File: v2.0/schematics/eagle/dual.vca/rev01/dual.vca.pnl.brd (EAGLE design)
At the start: 100 x 80 mm, 30 parts, among them J1 CV1, J10 CV4, J11 IN4, J12 OUT4, J2 IN1, J3 OUT1, J4 CV2, J5 IN2, J6 OUT2, J7 CV3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

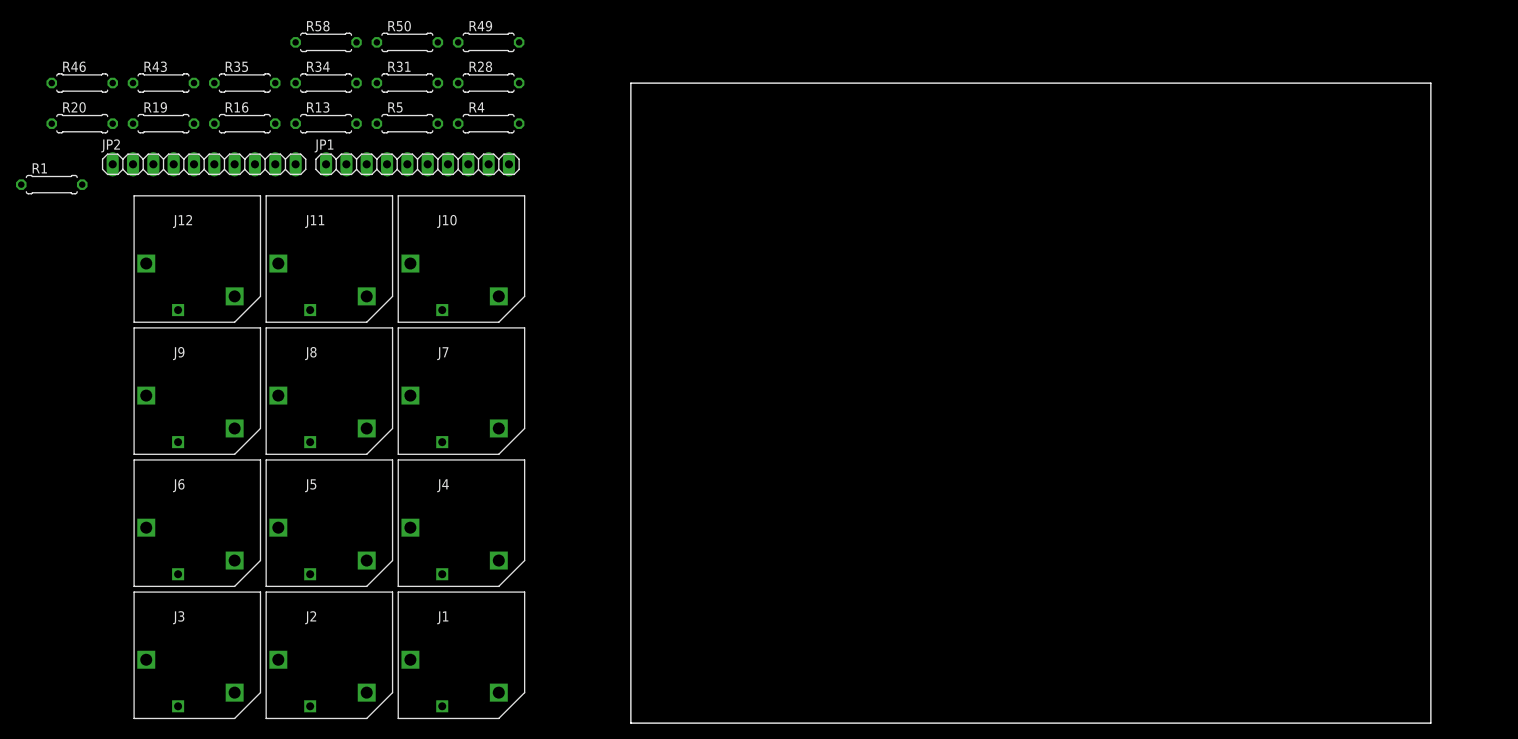
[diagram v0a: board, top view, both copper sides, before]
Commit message: Iniital board layout for main dual.vca
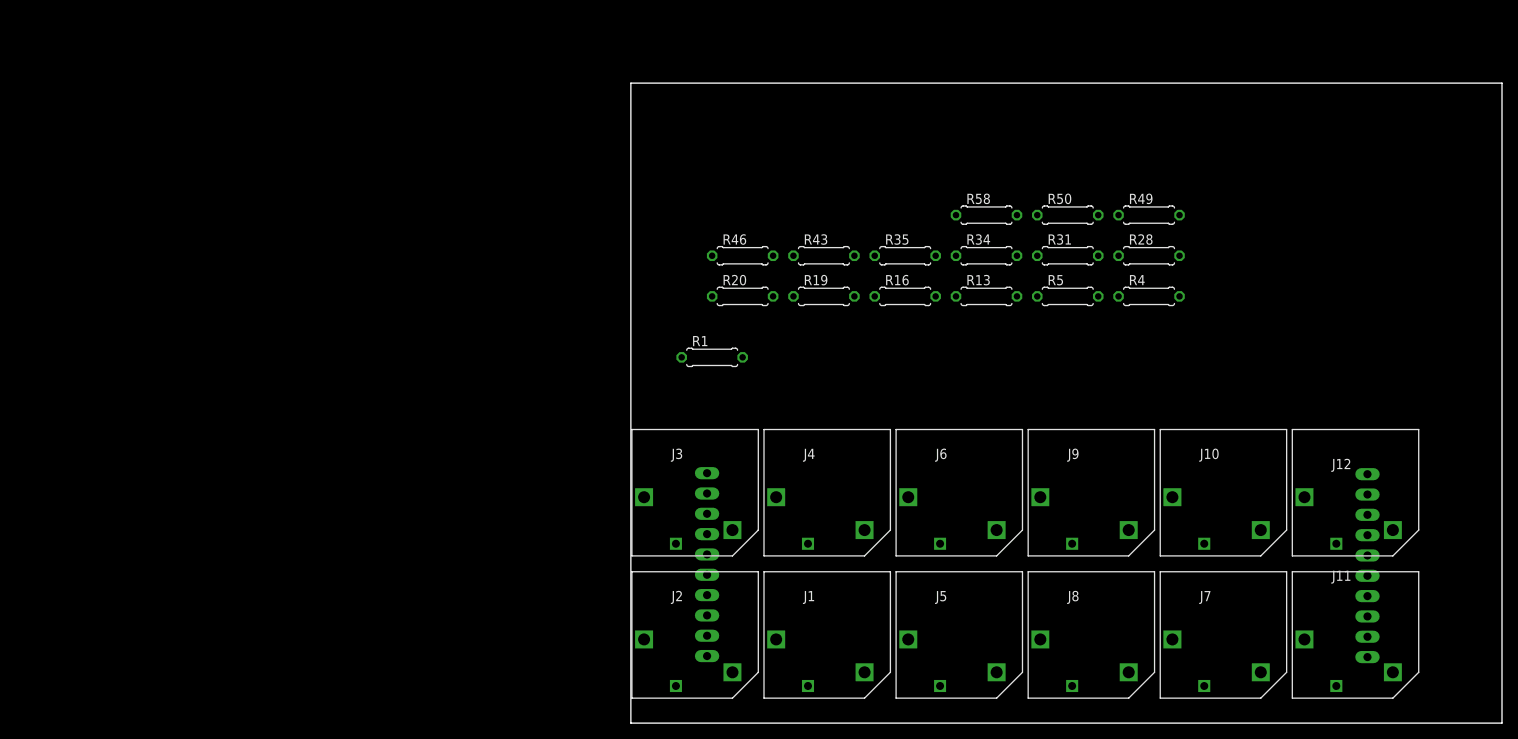
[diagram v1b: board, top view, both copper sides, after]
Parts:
- moved JP2 153.8 mm to (92.1, 19.7), flipped to the bottom, turned to 90 degrees
- moved J12 147.7 mm to (95.2, 24.1)
- moved J11 136.6 mm to (95.2, 6.35)
- moved J9 112.5 mm to (62.2, 24.1)
- moved J7 100.0 mm to (78.7, 6.35)
- moved J8 100.0 mm to (62.2, 6.35)
- moved J10 99.6 mm to (78.7, 24.1)
- moved J6 95.3 mm to (45.7, 24.1)
- moved R13 85.3 mm to (44.5, 53.3)
- moved R34 85.3 mm to (44.5, 58.4)
- moved R58 85.3 mm to (44.5, 63.5)
- moved R1 85.3 mm to (10.2, 45.7)
- moved R16 85.3 mm to (34.3, 53.3)
- moved R19 85.3 mm to (24.1, 53.3)
- moved R20 85.3 mm to (14.0, 53.3)
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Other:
- board size 100 x 80 mm -> 108.9 x 80 mm

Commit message: Added cam files; annotate panel schem with board edits; update cv resistor values
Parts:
- removed R1, R16, R31, R46: 100K, resistor:0207/7
- removed R20, R35, R5, R50: 1K, resistor:0207/7
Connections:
- removed net N$6: J10.P$3, R46.2
- net 0V: no longer R20.1, R35.1, R5.1, R50.1
- net CV1: no longer R1.1
- net CV2: no longer R16.1
- net CV3: no longer R31.1
- net CV4: now also J10.P$3; no longer R46.1
- net IN1: no longer R5.2
- net IN2: no longer R20.2
- net IN3: no longer R35.2
- net IN4: no longer R50.2
- net N$16: no longer R1.2
- net N$7: no longer R31.2
- net N$8: no longer R16.2
